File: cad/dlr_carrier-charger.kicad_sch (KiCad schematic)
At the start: 25 parts, among them J1 PV_IN, Q1 DMN4035L-7, Q2 DMN4035L-7, U8 BQ24650RVAR

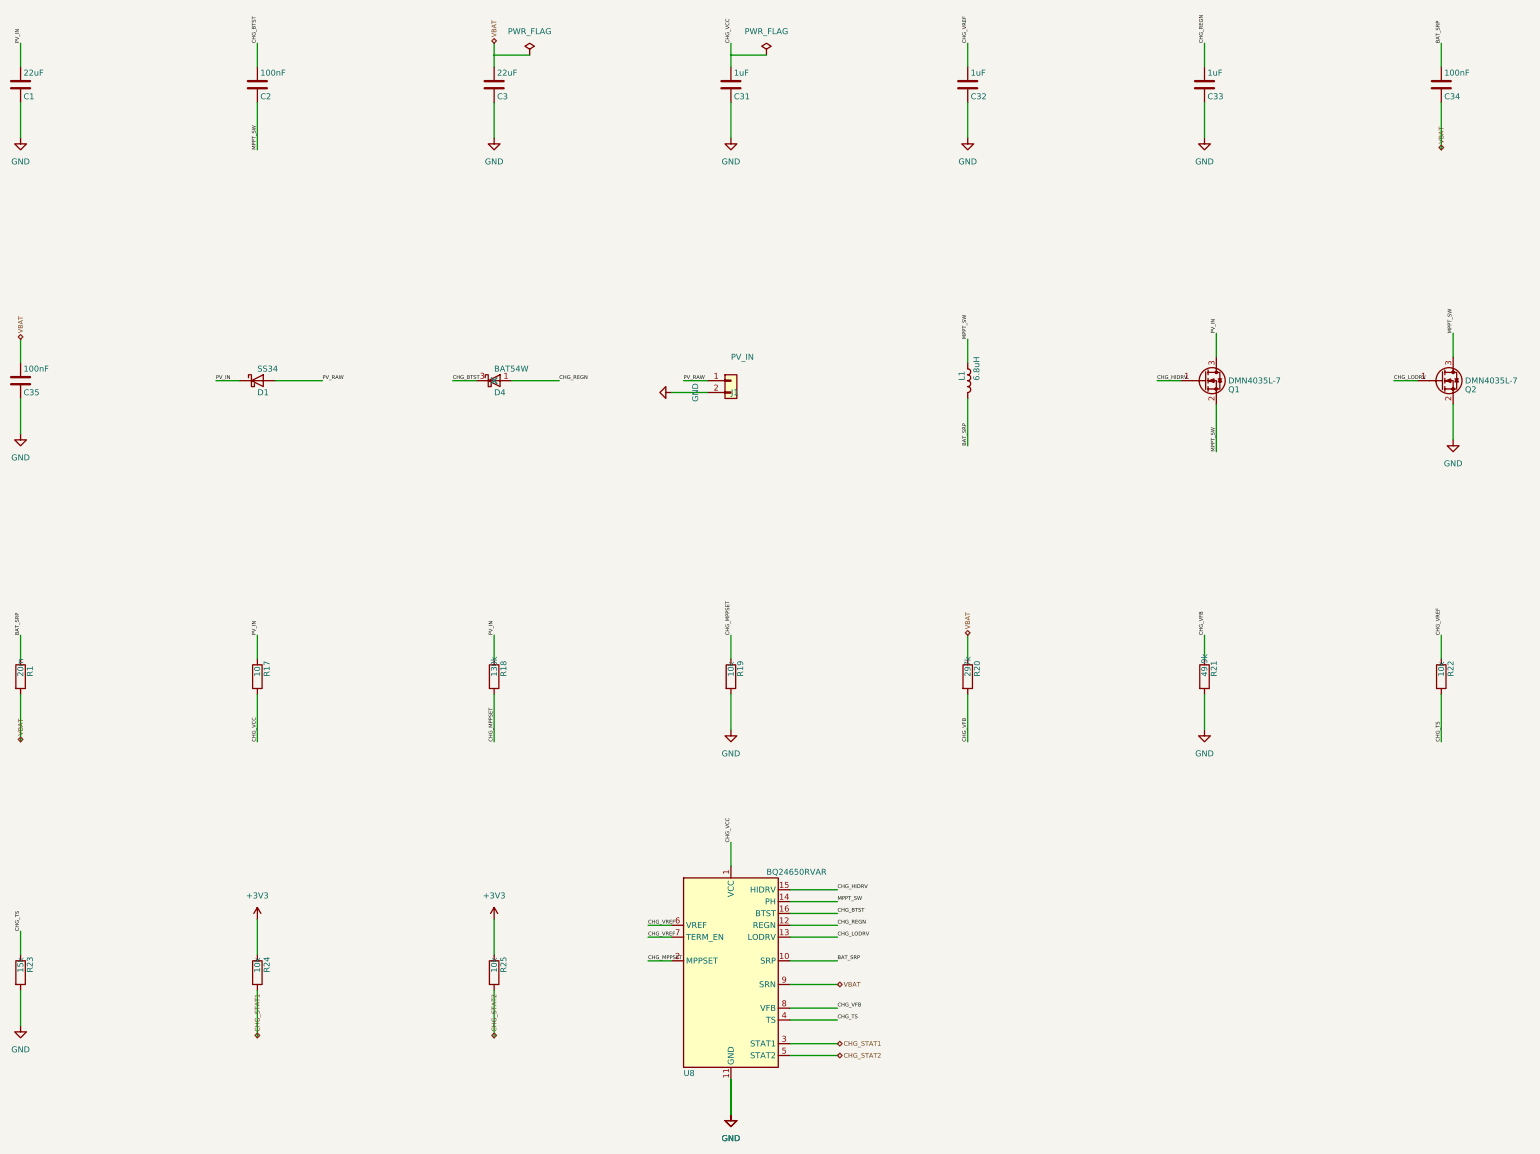
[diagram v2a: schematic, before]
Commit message: 🩺 refactor(schematic): cross-sheet nets via global labels, no sheet pins
Three attempts at making the hierarchical sheet-pin mechanism pass KiCad 9 failed
(project name, instance paths, label type), so the mechanism goes. Cross-sheet nets
now connect by name through global labels on the child sheets; the root carries
sheet symbols only — no pins, no stub wires, no labels.

That removes the whole hier_label_mismatch / label_dangling class rather than
chasing it, and it matches the connectivity style the generate-schematic skill
already prescribes for this project ("all inter-block connections use net labels").

kicad-sch-api's add_global_label still does not serialize, so the labels are emitted
as hierarchical and rewritten in the saved sheet.

Co-Authored-By: Claude Opus 5 <noreply@anthropic.com>
Claude-Session: https://claude.ai/code/session_011xr7VCL7rkJj2WE2uQF7sF
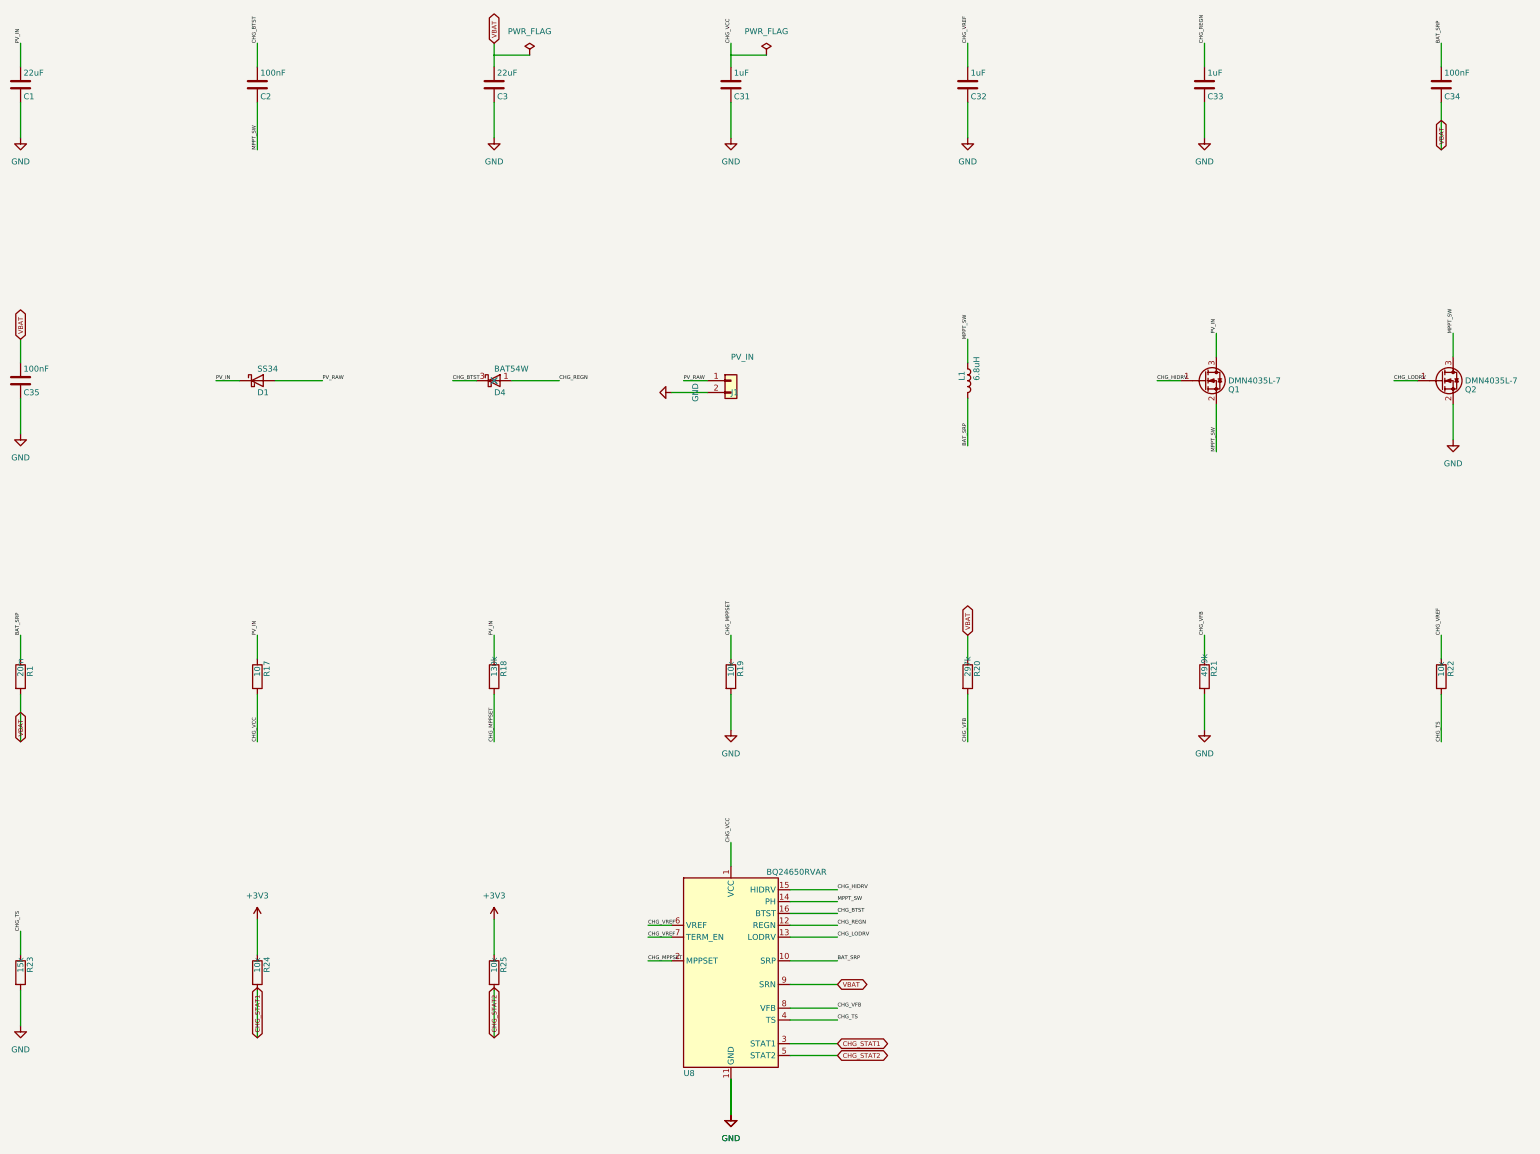
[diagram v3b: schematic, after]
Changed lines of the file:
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@@
 		(instances
 			(project "SOLAR MPPT CHARGER"
-				(path "/40c61e59-64f7-482c-bac7-2bc5cddc1686"
+				(path "/d9659de3-5829-484a-82b7-53bebe63b378"
 					(reference "C1")
 					(unit 1)
@@
 		(instances
 			(project "SOLAR MPPT CHARGER"
-				(path "/40c61e59-64f7-482c-bac7-2bc5cddc1686"
+				(path "/d9659de3-5829-484a-82b7-53bebe63b378"
 					(reference "C2")
 					(unit 1)
@@
 		(instances
 			(project "SOLAR MPPT CHARGER"
-				(path "/40c61e59-64f7-482c-bac7-2bc5cddc1686"
+				(path "/d9659de3-5829-484a-82b7-53bebe63b378"
 					(reference "C3")
 					(unit 1)
@@
 		(instances
 			(project "SOLAR MPPT CHARGER"
-				(path "/40c61e59-64f7-482c-bac7-2bc5cddc1686"
+				(path "/d9659de3-5829-484a-82b7-53bebe63b378"
 					(reference "C31")
 					(unit 1)
@@
 		(instances
 			(project "SOLAR MPPT CHARGER"
-				(path "/40c61e59-64f7-482c-bac7-2bc5cddc1686"
+				(path "/d9659de3-5829-484a-82b7-53bebe63b378"
 					(reference "C32")
 					(unit 1)
@@
 		(instances
 			(project "SOLAR MPPT CHARGER"
-				(path "/40c61e59-64f7-482c-bac7-2bc5cddc1686"
+				(path "/d9659de3-5829-484a-82b7-53bebe63b378"
 					(reference "C33")
 					(unit 1)
@@
 		(instances
 			(project "SOLAR MPPT CHARGER"
-				(path "/40c61e59-64f7-482c-bac7-2bc5cddc1686"
+				(path "/d9659de3-5829-484a-82b7-53bebe63b378"
 					(reference "C34")
 					(unit 1)
@@
 		(instances
 			(project "SOLAR MPPT CHARGER"
-				(path "/40c61e59-64f7-482c-bac7-2bc5cddc1686"
+				(path "/d9659de3-5829-484a-82b7-53bebe63b378"
 					(reference "C35")
 					(unit 1)
@@
 		(instances
 			(project "SOLAR MPPT CHARGER"
-				(path "/40c61e59-64f7-482c-bac7-2bc5cddc1686"
+				(path "/d9659de3-5829-484a-82b7-53bebe63b378"
 					(reference "D1")
 					(unit 1)
@@
 		(instances
 			(project "SOLAR MPPT CHARGER"
-				(path "/40c61e59-64f7-482c-bac7-2bc5cddc1686"
+				(path "/d9659de3-5829-484a-82b7-53bebe63b378"
 					(reference "D4")
 					(unit 1)
@@
 		(instances
 			(project "SOLAR MPPT CHARGER"
-				(path "/40c61e59-64f7-482c-bac7-2bc5cddc1686"
+				(path "/d9659de3-5829-484a-82b7-53bebe63b378"
 					(reference "J1")
 					(unit 1)
@@
 		(instances
 			(project "SOLAR MPPT CHARGER"
-				(path "/40c61e59-64f7-482c-bac7-2bc5cddc1686"
+				(path "/d9659de3-5829-484a-82b7-53bebe63b378"
 					(reference "L1")
 					(unit 1)
@@
 		(instances
 			(project "SOLAR MPPT CHARGER"
-				(path "/40c61e59-64f7-482c-bac7-2bc5cddc1686"
+				(path "/d9659de3-5829-484a-82b7-53bebe63b378"
 					(reference "Q1")
 					(unit 1)
@@
 		(instances
 			(project "SOLAR MPPT CHARGER"
-				(path "/40c61e59-64f7-482c-bac7-2bc5cddc1686"
+				(path "/d9659de3-5829-484a-82b7-53bebe63b378"
 					(reference "Q2")
 					(unit 1)
@@
 		(instances
 			(project "SOLAR MPPT CHARGER"
-				(path "/40c61e59-64f7-482c-bac7-2bc5cddc1686"
+				(path "/d9659de3-5829-484a-82b7-53bebe63b378"
 					(reference "R1")
 					(unit 1)
@@
 		(instances
 			(project "SOLAR MPPT CHARGER"
-				(path "/40c61e59-64f7-482c-bac7-2bc5cddc1686"
+				(path "/d9659de3-5829-484a-82b7-53bebe63b378"
 					(reference "R17")
 					(unit 1)
@@
 		(instances
 			(project "SOLAR MPPT CHARGER"
-				(path "/40c61e59-64f7-482c-bac7-2bc5cddc1686"
+				(path "/d9659de3-5829-484a-82b7-53bebe63b378"
 					(reference "R18")
 					(unit 1)
@@
 		(instances
 			(project "SOLAR MPPT CHARGER"
-				(path "/40c61e59-64f7-482c-bac7-2bc5cddc1686"
+				(path "/d9659de3-5829-484a-82b7-53bebe63b378"
 					(reference "R19")
 					(unit 1)
@@
 		(instances
 			(project "SOLAR MPPT CHARGER"
-				(path "/40c61e59-64f7-482c-bac7-2bc5cddc1686"
+				(path "/d9659de3-5829-484a-82b7-53bebe63b378"
 					(reference "R20")
 					(unit 1)
@@
 		(instances
 			(project "SOLAR MPPT CHARGER"
-				(path "/40c61e59-64f7-482c-bac7-2bc5cddc1686"
+				(path "/d9659de3-5829-484a-82b7-53bebe63b378"
 					(reference "R21")
 					(unit 1)
@@
 		(instances
 			(project "SOLAR MPPT CHARGER"
-				(path "/40c61e59-64f7-482c-bac7-2bc5cddc1686"
+				(path "/d9659de3-5829-484a-82b7-53bebe63b378"
 					(reference "R22")
 					(unit 1)
@@
 		(instances
 			(project "SOLAR MPPT CHARGER"
-				(path "/40c61e59-64f7-482c-bac7-2bc5cddc1686"
+				(path "/d9659de3-5829-484a-82b7-53bebe63b378"
 					(reference "R23")
 					(unit 1)
@@
 		(instances
 			(project "SOLAR MPPT CHARGER"
-				(path "/40c61e59-64f7-482c-bac7-2bc5cddc1686"
+				(path "/d9659de3-5829-484a-82b7-53bebe63b378"
 					(reference "R24")
 					(unit 1)
@@
 		(instances
 			(project "SOLAR MPPT CHARGER"
-				(path "/40c61e59-64f7-482c-bac7-2bc5cddc1686"
+				(path "/d9659de3-5829-484a-82b7-53bebe63b378"
 					(reference "R25")
 					(unit 1)
@@
 		(instances
 			(project "SOLAR MPPT CHARGER"
-				(path "/40c61e59-64f7-482c-bac7-2bc5cddc1686"
+				(path "/d9659de3-5829-484a-82b7-53bebe63b378"
 					(reference "U8")
 					(unit 1)
@@
 		(instances
 			(project "SOLAR MPPT CHARGER"
-				(path "/40c61e59-64f7-482c-bac7-2bc5cddc1686"
+				(path "/d9659de3-5829-484a-82b7-53bebe63b378"
 					(reference "#PWR001")
 					(unit 1)
@@
 		(instances
 			(project "SOLAR MPPT CHARGER"
-				(path "/40c61e59-64f7-482c-bac7-2bc5cddc1686"
+				(path "/d9659de3-5829-484a-82b7-53bebe63b378"
 					(reference "#PWR002")
 					(unit 1)
@@
 		(instances
 			(project "SOLAR MPPT CHARGER"
-				(path "/40c61e59-64f7-482c-bac7-2bc5cddc1686"
+				(path "/d9659de3-5829-484a-82b7-53bebe63b378"
 					(reference "#FLG001")
 					(unit 1)
@@
 		(instances
 			(project "SOLAR MPPT CHARGER"
-				(path "/40c61e59-64f7-482c-bac7-2bc5cddc1686"
+				(path "/d9659de3-5829-484a-82b7-53bebe63b378"
 					(reference "#PWR003")
 					(unit 1)
@@
 		(instances
 			(project "SOLAR MPPT CHARGER"
-				(path "/40c61e59-64f7-482c-bac7-2bc5cddc1686"
+				(path "/d9659de3-5829-484a-82b7-53bebe63b378"
 					(reference "#PWR004")
 					(unit 1)
@@
 		(instances
 			(project "SOLAR MPPT CHARGER"
-				(path "/40c61e59-64f7-482c-bac7-2bc5cddc1686"
+				(path "/d9659de3-5829-484a-82b7-53bebe63b378"
 					(reference "#PWR005")
 					(unit 1)
@@
 		(instances
 			(project "SOLAR MPPT CHARGER"
-				(path "/40c61e59-64f7-482c-bac7-2bc5cddc1686"
+				(path "/d9659de3-5829-484a-82b7-53bebe63b378"
 					(reference "#PWR006")
 					(unit 1)
@@
 		(instances
 			(project "SOLAR MPPT CHARGER"
-				(path "/40c61e59-64f7-482c-bac7-2bc5cddc1686"
+				(path "/d9659de3-5829-484a-82b7-53bebe63b378"
 					(reference "#PWR007")
 					(unit 1)
@@
 		(instances
 			(project "SOLAR MPPT CHARGER"
-				(path "/40c61e59-64f7-482c-bac7-2bc5cddc1686"
+				(path "/d9659de3-5829-484a-82b7-53bebe63b378"
 					(reference "#PWR008")
 					(unit 1)
@@
 		(instances
 			(project "SOLAR MPPT CHARGER"
-				(path "/40c61e59-64f7-482c-bac7-2bc5cddc1686"
+				(path "/d9659de3-5829-484a-82b7-53bebe63b378"
 					(reference "#PWR009")
 					(unit 1)
@@
 		(instances
 			(project "SOLAR MPPT CHARGER"
-				(path "/40c61e59-64f7-482c-bac7-2bc5cddc1686"
+				(path "/d9659de3-5829-484a-82b7-53bebe63b378"
 					(reference "#PWR010")
 					(unit 1)
@@
 		(instances
 			(project "SOLAR MPPT CHARGER"
-				(path "/40c61e59-64f7-482c-bac7-2bc5cddc1686"
+				(path "/d9659de3-5829-484a-82b7-53bebe63b378"
 					(reference "#PWR011")
 					(unit 1)
@@
 		(instances
 			(project "SOLAR MPPT CHARGER"
-				(path "/40c61e59-64f7-482c-bac7-2bc5cddc1686"
+				(path "/d9659de3-5829-484a-82b7-53bebe63b378"
 					(reference "#PWR012")
 					(unit 1)
@@
 		(instances
 			(project "SOLAR MPPT CHARGER"
-				(path "/40c61e59-64f7-482c-bac7-2bc5cddc1686"
+				(path "/d9659de3-5829-484a-82b7-53bebe63b378"
 					(reference "#PWR013")
 					(unit 1)
@@
 		(instances
 			(project "SOLAR MPPT CHARGER"
-				(path "/40c61e59-64f7-482c-bac7-2bc5cddc1686"
+				(path "/d9659de3-5829-484a-82b7-53bebe63b378"
 					(reference "#PWR014")
 					(unit 1)
@@
 		(instances
 			(project "SOLAR MPPT CHARGER"
-				(path "/40c61e59-64f7-482c-bac7-2bc5cddc1686"
+				(path "/d9659de3-5829-484a-82b7-53bebe63b378"
 					(reference "#PWR015")
 					(unit 1)
@@
 		(instances
 			(project "SOLAR MPPT CHARGER"
-				(path "/40c61e59-64f7-482c-bac7-2bc5cddc1686"
+				(path "/d9659de3-5829-484a-82b7-53bebe63b378"
 					(reference "#FLG002")
 					(unit 1)
@@
 		)
 	)
-	(hierarchical_label "CHG_STAT1"
+	(global_label "CHG_STAT1"
 		(shape bidirectional)
 		(at 114.3 274.32 270)
@@
 		)
 	)
-	(hierarchical_label "CHG_STAT1"
+	(global_label "CHG_STAT1"
 		(shape bidirectional)
 		(at 238.76 275.59 0)
@@
 		)
 	)
-	(hierarchical_label "CHG_STAT2"
+	(global_label "CHG_STAT2"
 		(shape bidirectional)
 		(at 165.1 274.32 270)
@@
 		)
 	)
-	(hierarchical_label "CHG_STAT2"
+	(global_label "CHG_STAT2"
 		(shape bidirectional)
 		(at 238.76 278.13 0)
@@
 		)
 	)
-	(hierarchical_label "VBAT"
+	(global_label "VBAT"
 		(shape bidirectional)
 		(at 165.1 60.96 90)
@@
 		)
 	)
-	(hierarchical_label "VBAT"
+	(global_label "VBAT"
 		(shape bidirectional)
 		(at 368.3 83.82 270)
@@
 		)
 	)
-	(hierarchical_label "VBAT"
+	(global_label "VBAT"
 		(shape bidirectional)
 		(at 63.5 124.46 90)
@@
 		)
 	)
-	(hierarchical_label "VBAT"
+	(global_label "VBAT"
 		(shape bidirectional)
 		(at 63.5 210.82 270)
@@
 		)
 	)
-	(hierarchical_label "VBAT"
+	(global_label "VBAT"
 		(shape bidirectional)
 		(at 266.7 187.96 90)
@@
 		)
 	)
-	(hierarchical_label "VBAT"
+	(global_label "VBAT"
 		(shape bidirectional)
 		(at 238.76 262.89 0)
@@
 	)
 	(sheet_instances
-		(path "/ff7de960-6bdd-4734-b765-9a85f5be0719"
+		(path "/dbb449b7-0608-44b3-8ed5-90e8123dd821"
 			(page "2")
 		)
